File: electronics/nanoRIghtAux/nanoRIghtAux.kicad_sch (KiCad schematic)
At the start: 12 parts, among them J1 EA Graphic LCD, M1 HYDPRESS A, M2 HYDPRESS B, M3 FUEL QTY FWD, M4 FUEL QTY AFT, SW1 Reset Button, SW2 Zeroize Button, SW3 Zeroize Sensor, U1 MM5451YN, U2 MAX7219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

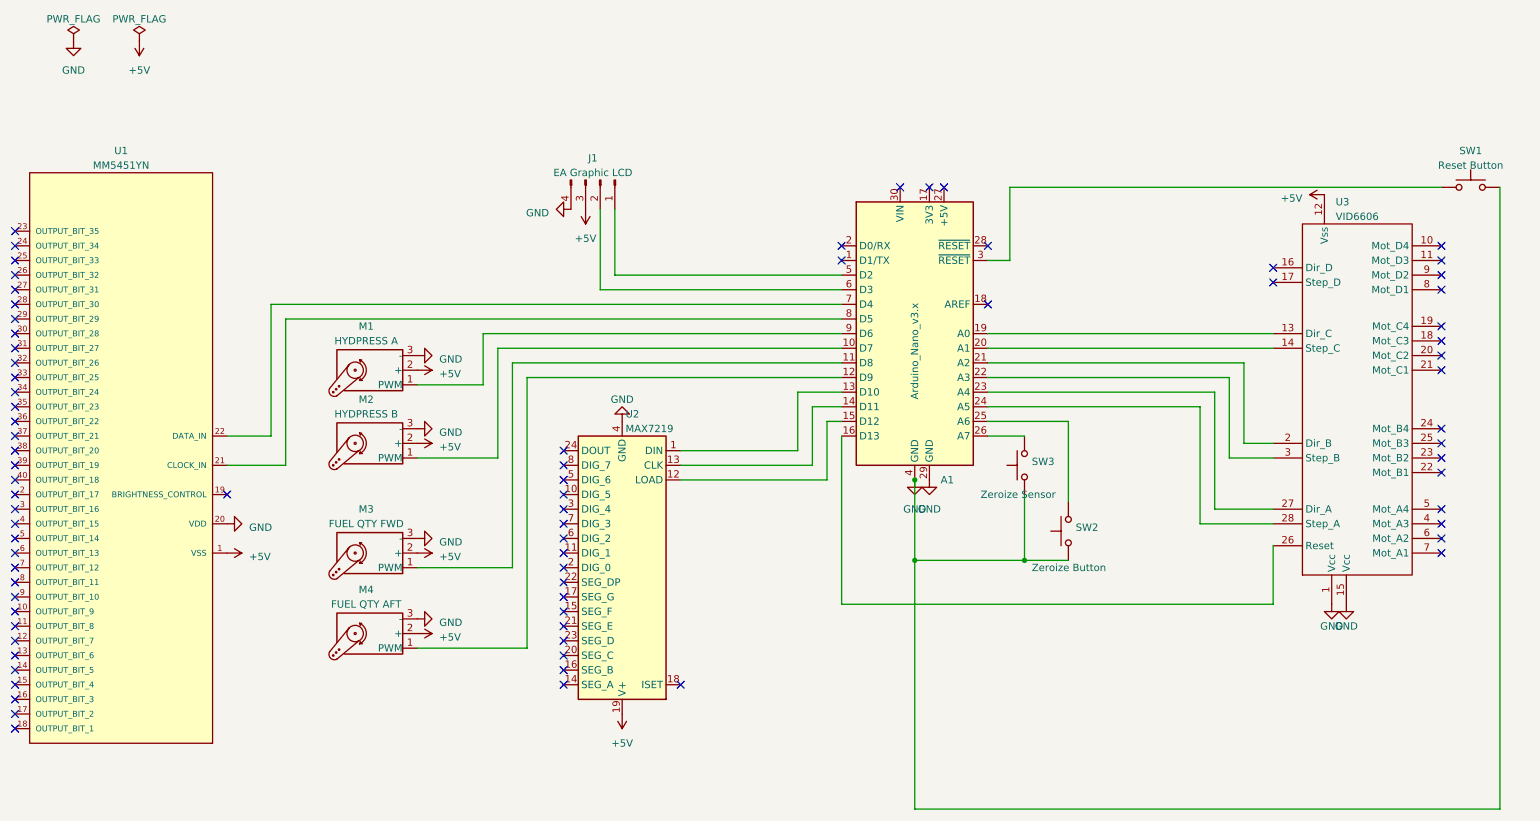
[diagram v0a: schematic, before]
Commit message: started adding connectors
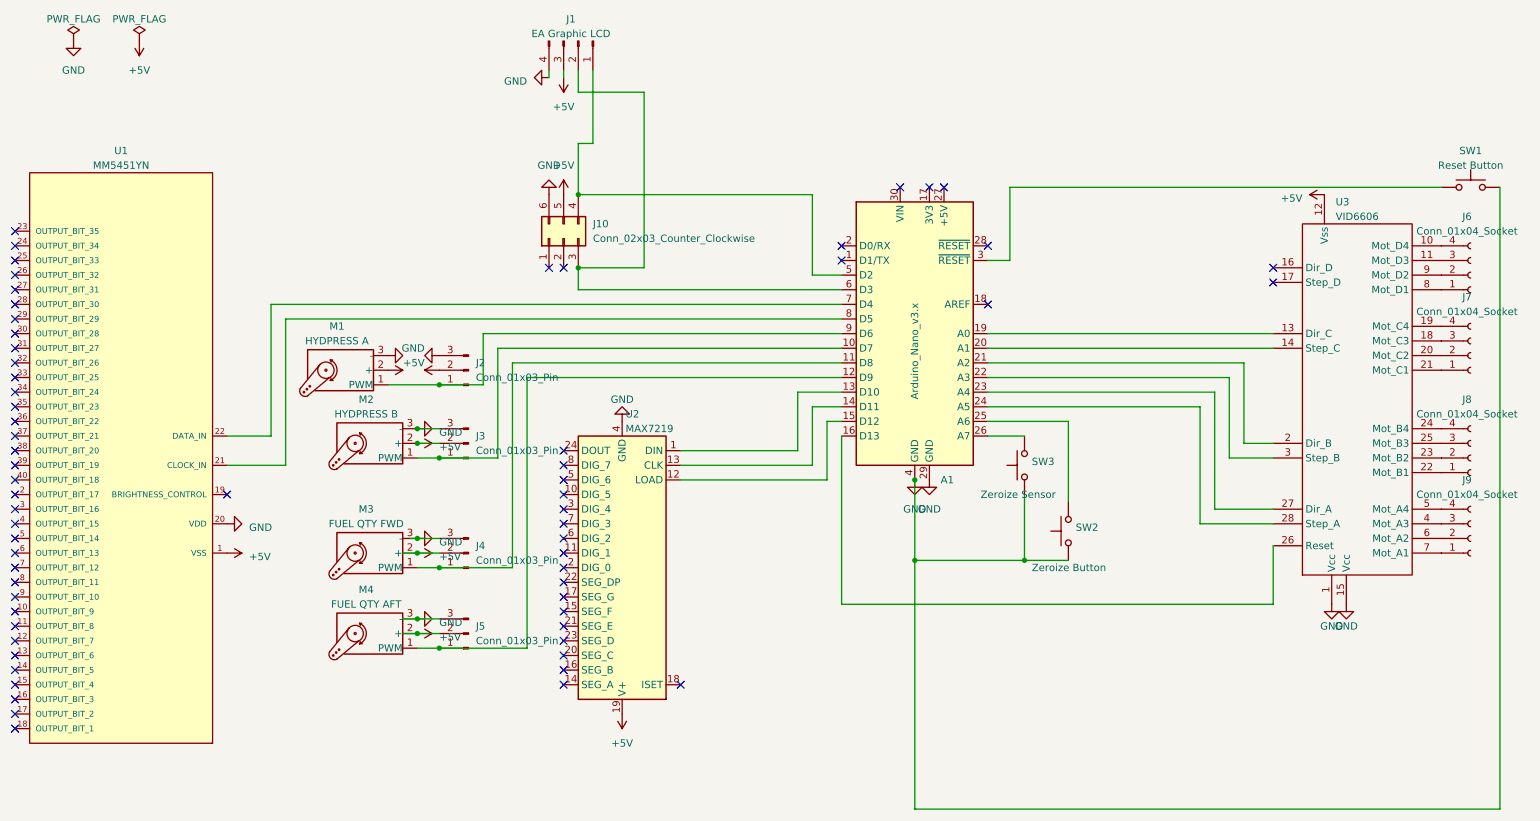
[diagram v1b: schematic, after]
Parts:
- added J10: Conn_02x03_Counter_Clockwise, symbol Connector_Generic:Conn_02x03_Counter_Clockwise
- added J2, J3, J4, J5: Conn_01x03_Pin, symbol Connector:Conn_01x03_Pin
- added J6, J7, J8, J9: Conn_01x04_Socket, symbol Connector:Conn_01x04_Socket
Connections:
- net +5V: now also J10.5 (Pin_5), J2.2 (Pin_2), J3.2 (Pin_2), J4.2 (Pin_2), J5.2 (Pin_2)
- net GND: now also J10.6 (Pin_6), J2.3 (Pin_3), J3.3 (Pin_3), J4.3 (Pin_3), J5.3 (Pin_3)
- net at A1.9 (D6), M1.1 (PWM): now also J2.1 (Pin_1)
- net at A1.12 (D9), M4.1 (PWM): now also J5.1 (Pin_1)
- net at A1.5 (D2), J1.1 (Pin_1): now also J10.4 (Pin_4)
- net at A1.6 (D3), J1.2 (Pin_2): now also J10.3 (Pin_3)
- net at A1.10 (D7), M2.1 (PWM): now also J3.1 (Pin_1)
- net at U3.10 (Mot_D4): now also J6.4 (Pin_4)
- net at U3.11 (Mot_D3): now also J6.3 (Pin_3)
- net at U3.18 (Mot_C3): now also J7.3 (Pin_3)
- net at U3.19 (Mot_C4): now also J7.4 (Pin_4)
- net at U3.20 (Mot_C2): now also J7.2 (Pin_2)
- net at U3.21 (Mot_C1): now also J7.1 (Pin_1)
- net at U3.22 (Mot_B1): now also J8.1 (Pin_1)
- net at U3.23 (Mot_B2): now also J8.2 (Pin_2)
- net at U3.24 (Mot_B4): now also J8.4 (Pin_4)
- net at U3.25 (Mot_B3): now also J8.3 (Pin_3)
- net at U3.4 (Mot_A3): now also J9.3 (Pin_3)
- net at U3.5 (Mot_A4): now also J9.4 (Pin_4)
- net at U3.6 (Mot_A2): now also J9.2 (Pin_2)
- net at U3.7 (Mot_A1): now also J9.1 (Pin_1)
- net at U3.8 (Mot_D1): now also J6.1 (Pin_1)
- net at U3.9 (Mot_D2): now also J6.2 (Pin_2)
- net at A1.11 (D8), M3.1 (PWM): now also J4.1 (Pin_1)
- no-connect marks 79 -> 65
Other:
- moved on the sheet: J1, M1

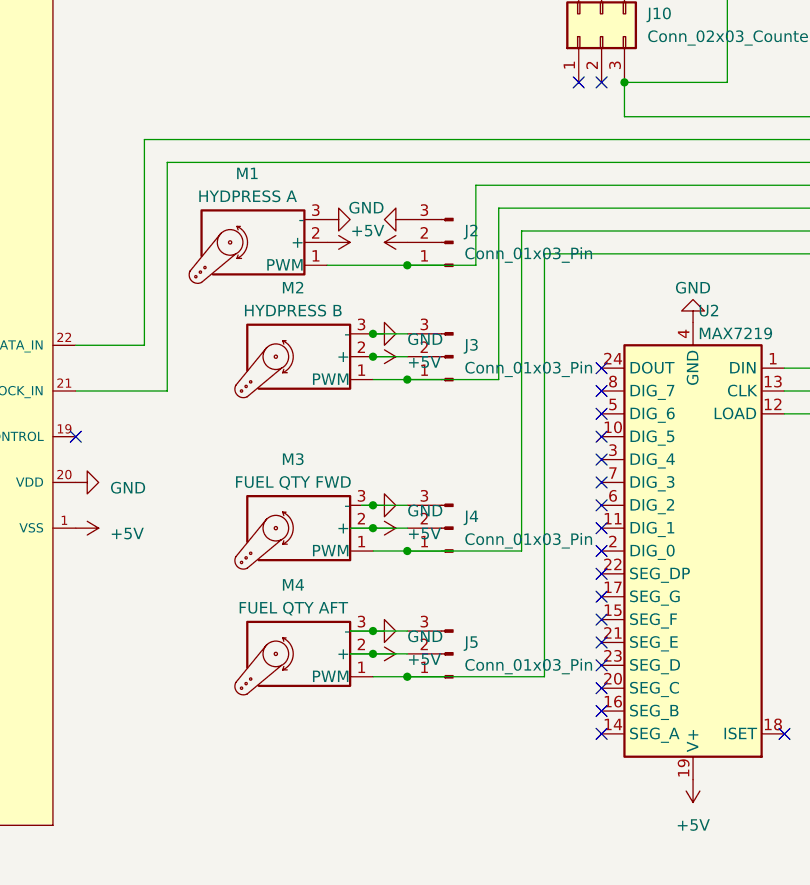
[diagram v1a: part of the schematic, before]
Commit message: removed servos, connectors only
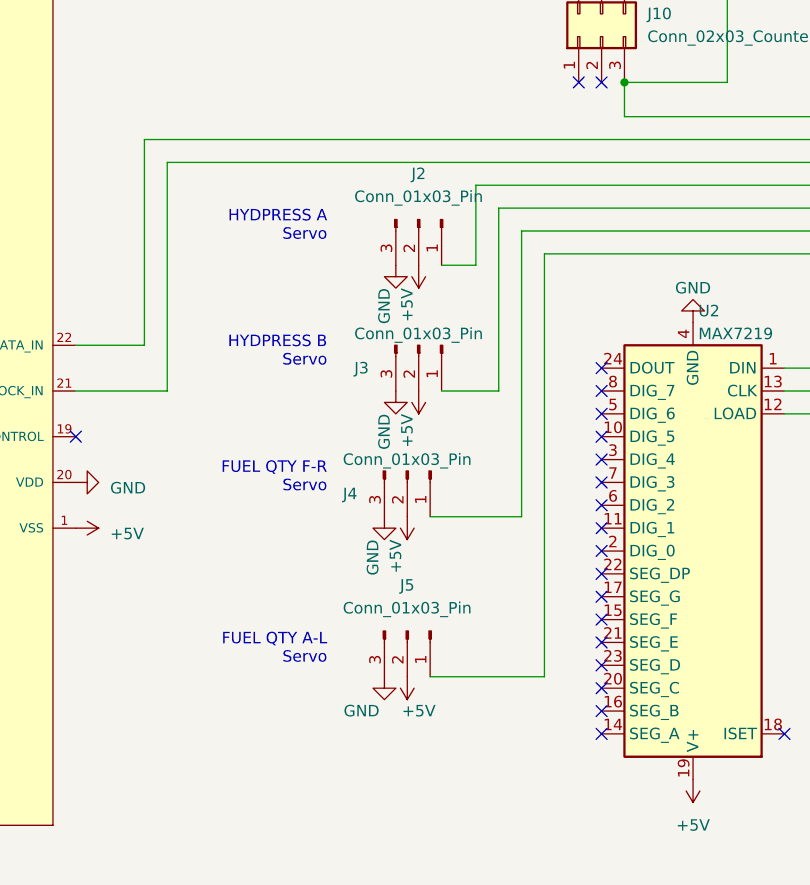
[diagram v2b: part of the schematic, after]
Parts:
- removed M1: HYDPRESS A, symbol Motor:Motor_Servo
- removed M2: HYDPRESS B, symbol Motor:Motor_Servo
- removed M3: FUEL QTY FWD, symbol Motor:Motor_Servo
- removed M4: FUEL QTY AFT, symbol Motor:Motor_Servo
- J10: footprint (none) -> Connector_PinHeader_2.54mm:PinHeader_2x03_P2.54mm_Vertical
- J2, J3, J4, J5: footprint (none) -> Connector_PinHeader_2.54mm:PinHeader_1x03_P2.54mm_Vertical
- J6, J7, J8, J9: footprint (none) -> Connector_PinHeader_2.54mm:PinHeader_1x04_P2.54mm_Vertical
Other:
- note added: "FUEL QTY A-L Servo"
- note added: "FUEL QTY F-R Servo"
- note added: "HYDPRESS A Servo"
- note added: "HYDPRESS B Servo"
- moved on the sheet: J2, J3, J4, J5

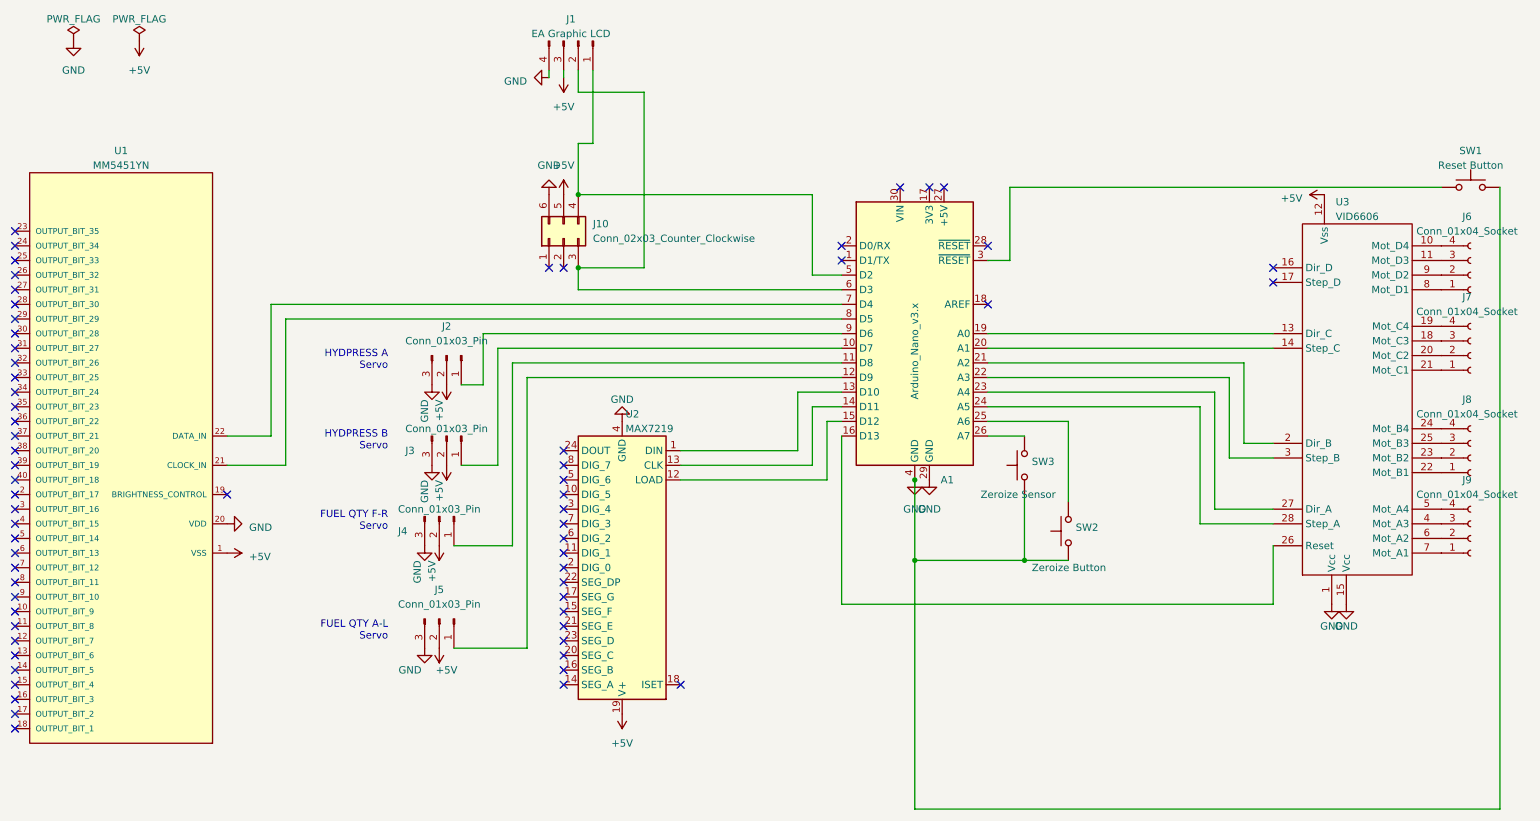
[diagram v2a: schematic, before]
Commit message: exchanged all parts with connectors
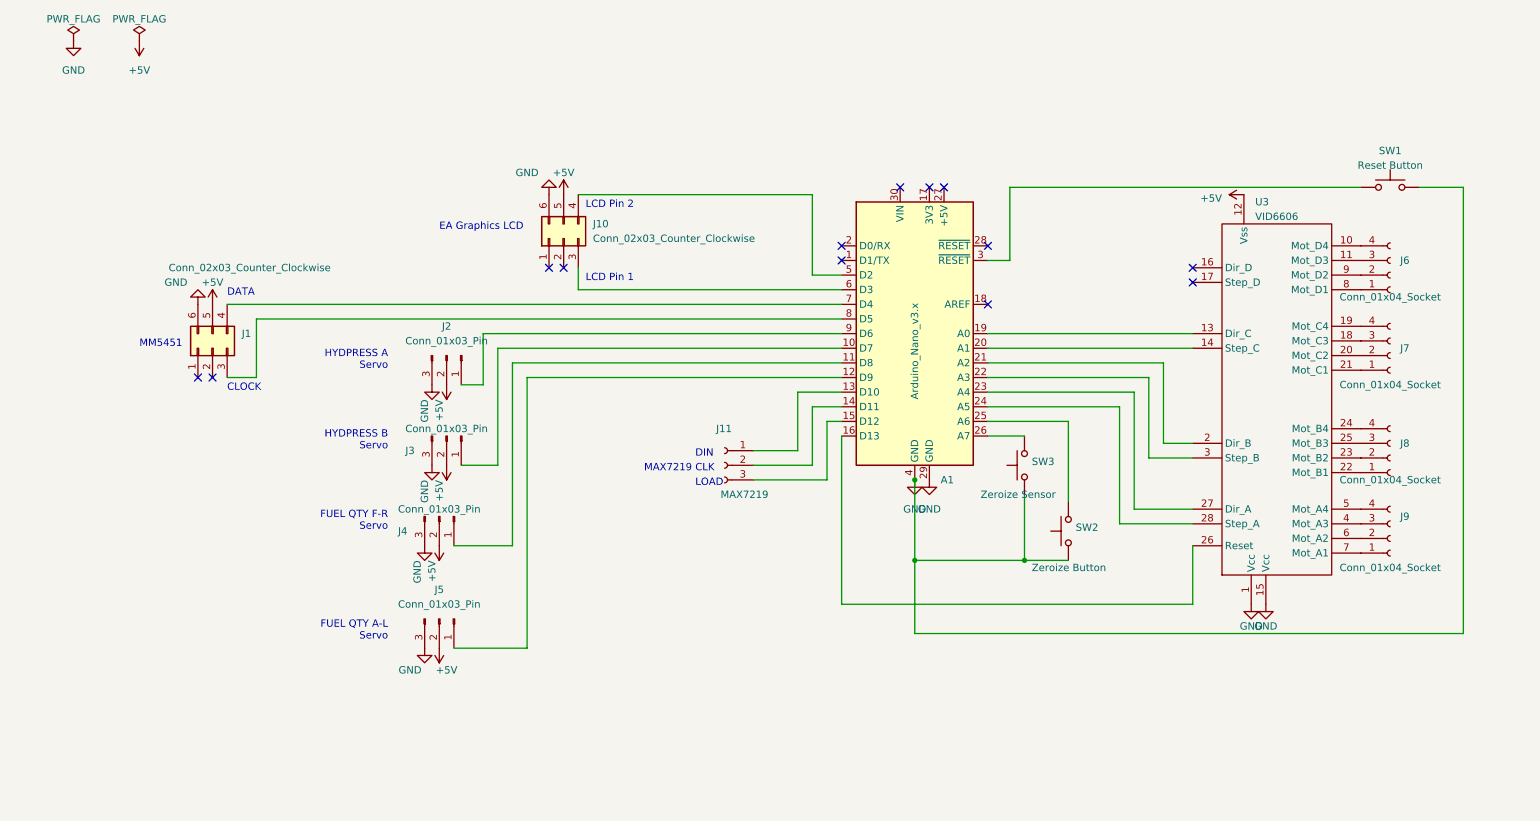
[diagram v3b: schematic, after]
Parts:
- removed J1: EA Graphic LCD, symbol Connector:Conn_01x04_Pin
- removed U1: MM5451YN, Micrel-PDIP-40LD-PL-1-0-0-*, symbol eec:MM5451YN
- removed U2: MAX7219, symbol Driver_LED:MAX7219
- added J1: Conn_02x03_Counter_Clockwise, Connector_PinHeader_2.54mm:PinHeader_2x03_P2.54mm_Vertical, symbol Connector_Generic:Conn_02x03_Counter_Clockwise
- added J11: MAX7219, Connector_PinSocket_2.54mm:PinSocket_1x03_P2.54mm_Vertical, symbol Connector:Conn_01x03_Socket
- SW1, SW2, SW3: footprint (none) -> Button_Switch_THT:SW_PUSH_6mm
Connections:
- net +5V: now also J1.5 (Pin_5)
- net GND: now also J1.6 (Pin_6)
- net at A1.8 (D5): now also J1.3 (Pin_3)
- net at A1.7 (D4): now also J1.4 (Pin_4)
- net at A1.13 (D10): now also J11.1 (Pin_1)
- net at A1.15 (D12): now also J11.3 (Pin_3)
- net at A1.14 (D11): now also J11.2 (Pin_2)
- no-connect marks 65 -> 13
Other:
- note added: "CLK"
- note added: "CLOCK"
- note added: "DATA"
- note added: "DIN"
- note added: "EA Graphics LCD"
- note added: "LCD Pin 1"
- note added: "LCD Pin 2"
- note added: "LOAD"
- note added: "MAX7219"
- note added: "MM5451"
- moved on the sheet: J6, J7, J8, J9, SW1, U3

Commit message: connectors renamed
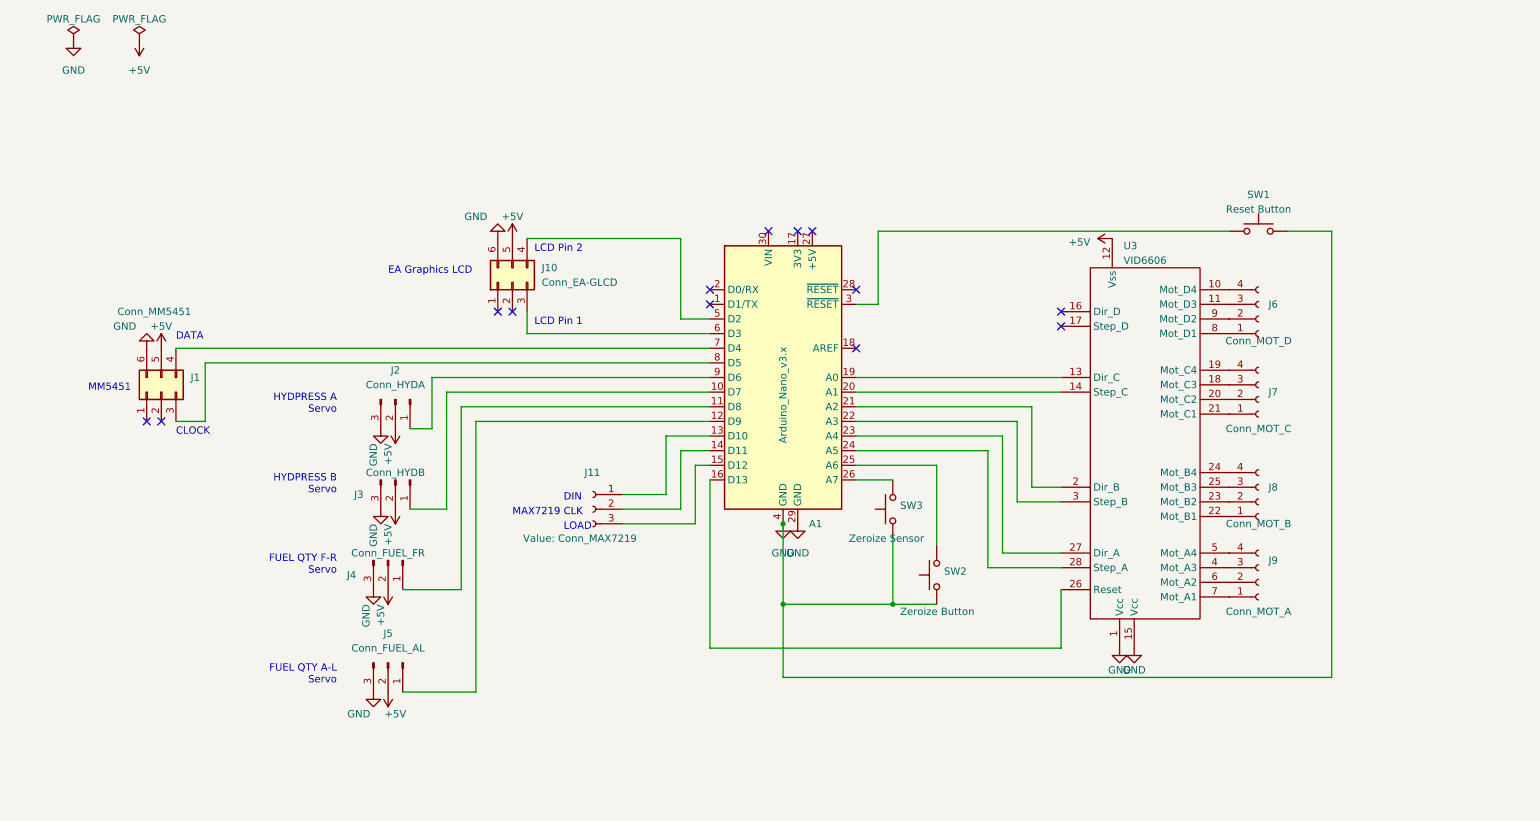
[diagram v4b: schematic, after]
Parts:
- J1: value Conn_02x03_Counter_Clockwise -> Conn_MM5451
- J10: value Conn_02x03_Counter_Clockwise -> Conn_EA-GLCD
- J11: value MAX7219 -> Conn_MAX7219
- J2: value Conn_01x03_Pin -> Conn_HYDA
- J3: value Conn_01x03_Pin -> Conn_HYDB
- J4: value Conn_01x03_Pin -> Conn_FUEL_FR
- J5: value Conn_01x03_Pin -> Conn_FUEL_AL
- J6: value Conn_01x04_Socket -> Conn_MOT_D
- J7: value Conn_01x04_Socket -> Conn_MOT_C
- J8: value Conn_01x04_Socket -> Conn_MOT_B
- J9: value Conn_01x04_Socket -> Conn_MOT_A
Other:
- moved on the sheet: A1, J1, J10, J11, J2, J3, J4, J5, J6, J7, J8, J9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
